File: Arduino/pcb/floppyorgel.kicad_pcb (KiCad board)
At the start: 2 copper layers, 50 x 50 mm, 44 parts, among them J1 VCC_Power_Select, J2 Floppy-Bus, J3 MAX485 Socket, J4 Floppy-Bus, J5 Buck-Converter-5V, J6 Buck-Converter-12V, J7 Floppy-Power, J8 IBM_PC_Floppy_IDC, J9 FTDI, SW1 Bus Address Select, SW2 Reset Button, U1 4021, U2 ATMEGA328P-AU, U3 24LC64, U4 74HC595, Y1 20 Mhz Crystal

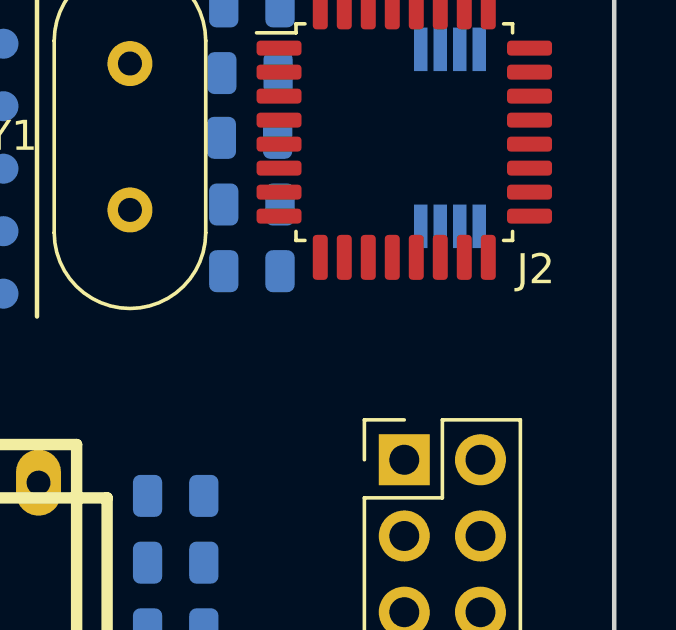
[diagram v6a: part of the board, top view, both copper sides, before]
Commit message: pcb: add testpads for I2C
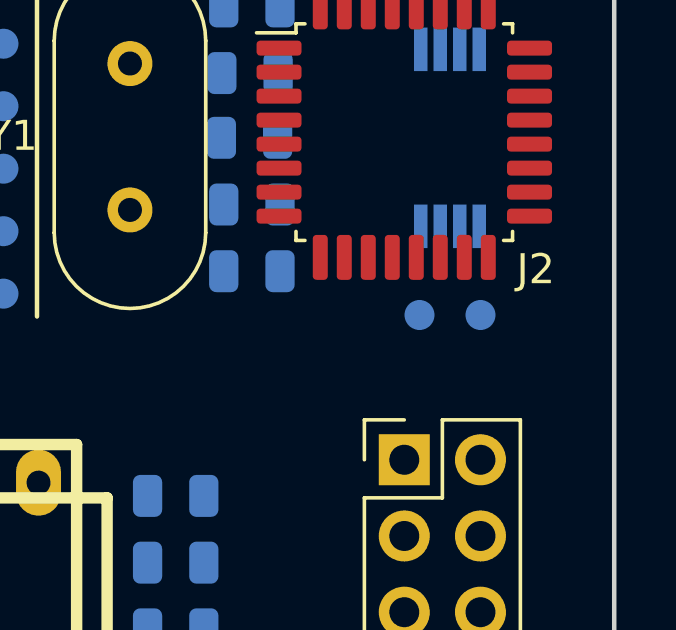
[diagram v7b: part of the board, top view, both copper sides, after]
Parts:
- added TP7: SDA, TestPoint:TestPoint_Pad_D1.0mm, B.Cu at (145.5, 118.1)
- added TP8: SCL, TestPoint:TestPoint_Pad_D1.0mm, B.Cu at (143.5, 118.1)
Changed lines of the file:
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@@
     (tracks 0)
     (zones 0)
-    (modules 44)
+    (modules 46)
     (nets 40)
   )
@@
       (net 9 GND))
   )
+  (module TestPoint:TestPoint_Pad_D1.0mm (layer B.Cu)
+    (at 145.542 118.11)
+    (descr "SMD pad as test Point, diameter 1.0mm")
+    (tags "test point SMD pad")
+    (attr virtual)
+    (fp_text reference TP7 (at 0 1.448) (layer B.Fab)
+      (effects (font (size 1 1) (thickness 0.15)) (justify mirror))
+    )
+    (fp_text value SDA (at 0 1.778 -90) (layer B.SilkS)
+      (effects (font (size 0.5 0.5) (thickness 0.125)) (justify mirror))
+    )
+    (fp_text user %R (at 0 1.45) (layer B.Fab)
+      (effects (font (size 1 1) (thickness 0.15)) (justify mirror))
+    )
+    (fp_circle (center 0 0) (end 1 0) (layer B.CrtYd) (width 0.05))
+    (fp_circle (center 0 0) (end 0 -0.7) (layer B.SilkS) (width 0.12))
+    (pad 1 smd circle (at 0 0) (size 1 1) (layers B.Cu B.Mask)
+      (net 32 /MCU/SDA))
+  )
+  (module TestPoint:TestPoint_Pad_D1.0mm (layer B.Cu)
+    (at 143.51 118.11)
+    (descr "SMD pad as test Point, diameter 1.0mm")
+    (tags "test point SMD pad")
+    (attr virtual)
+    (fp_text reference TP8 (at 0 1.448) (layer B.Fab)
+      (effects (font (size 1 1) (thickness 0.15)) (justify mirror))
+    )
+    (fp_text value SCL (at 0 1.778 -90) (layer B.SilkS)
+      (effects (font (size 0.5 0.5) (thickness 0.125)) (justify mirror))
+    )
+    (fp_circle (center 0 0) (end 0 -0.7) (layer B.SilkS) (width 0.12))
+    (fp_circle (center 0 0) (end 1 0) (layer B.CrtYd) (width 0.05))
+    (fp_text user %R (at 0 1.45) (layer B.Fab)
+      (effects (font (size 1 1) (thickness 0.15)) (justify mirror))
+    )
+    (pad 1 smd circle (at 0 0) (size 1 1) (layers B.Cu B.Mask)
+      (net 33 /MCU/SCL))
+  )
   (gr_line (start 130.7592 106.934) (end 130.7592 118.1608) (layer F.SilkS) (width 0.15))

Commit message: pcb: fix bus wiring, add bus silk pin descriptions
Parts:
- TP8: value SCL -> SDL
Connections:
- J2 pad 10: Net-(J2-Pad10) -> /Bus/BM
- J2 pad 2: Net-(J2-Pad2) -> /Bus/BUS_POWER
- J2 pad 4: Net-(J2-Pad4) -> GND
- J2 pad 7: Net-(J2-Pad7) -> /Bus/BP
- J2 pad 8: Net-(J2-Pad8) -> /Bus/BP
- J2 pad 9: Net-(J2-Pad9) -> /Bus/BM
- J3 pad 6: Net-(J2-Pad7) -> /Bus/BP
- J3 pad 7: Net-(J2-Pad9) -> /Bus/BM
- J4 pad 1: Net-(J2-Pad2) -> /Bus/BUS_POWER
- J4 pad 10: (no net) -> /Bus/BM
- J4 pad 2: (no net) -> /Bus/BUS_POWER
- J4 pad 3: Net-(J2-Pad4) -> GND
- J4 pad 4: (no net) -> GND
- J4 pad 7: Net-(J2-Pad8) -> /Bus/BP
- J4 pad 8: (no net) -> /Bus/BP
- J4 pad 9: Net-(J2-Pad10) -> /Bus/BM
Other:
- board text added: "20V"
- board text added: "BM"
- board text added: "BP"
- board text added: "GND"
- board text added: "N/C"
